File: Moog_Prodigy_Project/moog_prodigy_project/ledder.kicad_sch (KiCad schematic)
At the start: 44 parts, among them J6 NJ2FD-V, Q10 CA3046, Q11 BC327, Q8 BC556, Q9 CA3046, U1 LT1469, U15 LT1469, U16 LT1228, U17 NE5532

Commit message: Dodao u napomenu za linearne i logaritamske potenciometre, NE555 i sa 4007 semom spojena u jedno, dodati kvalitetni kondenzatori, ostao simbol za 4007 da izenim kao sto je jocke
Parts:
- added C77, C78: 100n, Capacitor_THT:CP_Radial_D5.0mm_P2.50mm, symbol Device:C
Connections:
- net +12V: now also C77.2, C78.2
- net GND: now also C77.1, C78.1
- net SIGNAL_OUT: no longer names the net of J6.S, RV16.2
- new net: Q8. (E), Q9., R97.2
- new net: CP1., Q9., R98.1
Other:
- note added: "IC1_1"
- note added: "IC1_2"
- note added: "IC1_3"
- note added: "IC1_4"
- note added: "IC1_5"
- note added: "IC2_1"
- note added: "IC2_2"
- note added: "IC2_3"
- note added: "IC2_4"
- note added: "IC2_5"
- note added: "NAPOMENA Kondenzatori: C71,C72,C73,C74,C75,C76,C77,C78 su vrednosti 100n i oni su kvalitetniji Ponteciometri: Linearni:RV12,RV15 Logaritamski: RV14,RV16"
- note added: "VOLUME MASTER"
- note removed: "NAPOMENA Kondenzatori: C71,C72,C73,C74,C75,C76 su vrednosti 100n i oni su kvalitetniji"
- title: (none) -> Dupli 3046 
- moved on the sheet: J6

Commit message: MOOG prodigy final 03.07.2026
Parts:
- R104, R105: value 6K81 -> 6K81 1%
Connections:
- new net: Q8. (E), Q9., R97.2
- new net: CP1., Q9., R98.1
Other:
- note added: "IC1"
- note added: "IC2"
- note added: "NAPOMENA 1 Kondenzatori: C71,C72,C73,C74,C75,C76,C77,C78 su vrednosti 100n i oni su kvalitetniji Ponteciometri: Linearni:RV12,RV15 Logaritamski: RV14,RV16"
- note added: "NAPOMENA 2 Otpornici cija je vrednost: 63K4, 18K2, 4K75, 6K81, 51M, 2.4M su otpornici iz E96 serije (1%) Ostali orpotnici su iz serije E24 (5%)"
- note removed: "NAPOMENA Kondenzatori: C71,C72,C73,C74,C75,C76,C77,C78 su vrednosti 100n i oni su kvalitetniji Ponteciometri: Linearni:RV12,RV15 Logaritamski: RV14,RV16"
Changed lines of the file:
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@@
 		(comment 4 "Miodrag Babić E1 87/2023")
 	)
+	(text "NAPOMENA 2\nOtpornici cija je vrednost:\n63K4, 18K2, 4K75, 6K81, 51M, 2.4M\nsu otpornici iz E96 serije (1%)\nOstali orpotnici su iz serije E24 (5%)"
+		(exclude_from_sim no)
+		(at 215.9 153.416 0)
+		(effects
+			(font
+				(size 1.27 1.27)
+				(thickness 0.254)
+				(bold yes)
+			)
+			(justify left)
+		)
+	)
 	(text "VCA\nBALANCE"
 		(exclude_from_sim no)
@@
 		)
 	)
-	(text "NAPOMENA\nKondenzatori:\nC71,C72,C73,C74,C75,C76,C77,C78\nsu vrednosti 100n i oni su kvalitetniji\n\nPonteciometri:\nLinearni:RV12,RV15\nLogaritamski: RV14,RV16"
+	(text "NAPOMENA 1\nKondenzatori:\nC71,C72,C73,C74,C75,C76,C77,C78\nsu vrednosti 100n i oni su kvalitetniji\n\nPonteciometri:\nLinearni:RV12,RV15\nLogaritamski: RV14,RV16"
 		(exclude_from_sim no)
-		(at 236.474 154.178 0)
+		(at 176.784 156.21 0)
 		(effects
 			(font
@@
 		)
 	)
+	(text "IC1"
+		(exclude_from_sim no)
+		(at 41.402 68.072 0)
+		(effects
+			(font
+				(size 1.27 1.27)
+			)
+		)
+	)
 	(text "IC2_2"
 		(exclude_from_sim no)
@@
 		)
 	)
+	(text "IC2"
+		(exclude_from_sim no)
+		(at 167.386 65.024 0)
+		(effects
+			(font
+				(size 1.27 1.27)
+			)
+		)
+	)
 	(text "EMPHASIS"
 		(exclude_from_sim no)
@@
 		)
 		(property "Value" "CA3046"
-			(at 50.038 76.962 90)
+			(at 41.91 70.358 90)
 			(effects
 				(font
@@
 		(dnp no)
 		(property "Reference" "R104"
-			(at 136.144 111.252 0)
+			(at 135.382 112.268 0)
 			(effects
 				(font
@@
 			)
 		)
-		(property "Value" "6K81"
-			(at 136.144 113.792 0)
+		(property "Value" "6K81 1%"
+			(at 131.826 114.554 0)
 			(effects
 				(font
@@
 			)
 		)
-		(property "Value" "6K81"
-			(at 151.384 120.142 90)
+		(property "Value" "6K81 1%"
+			(at 149.606 120.142 90)
 			(effects
 				(font

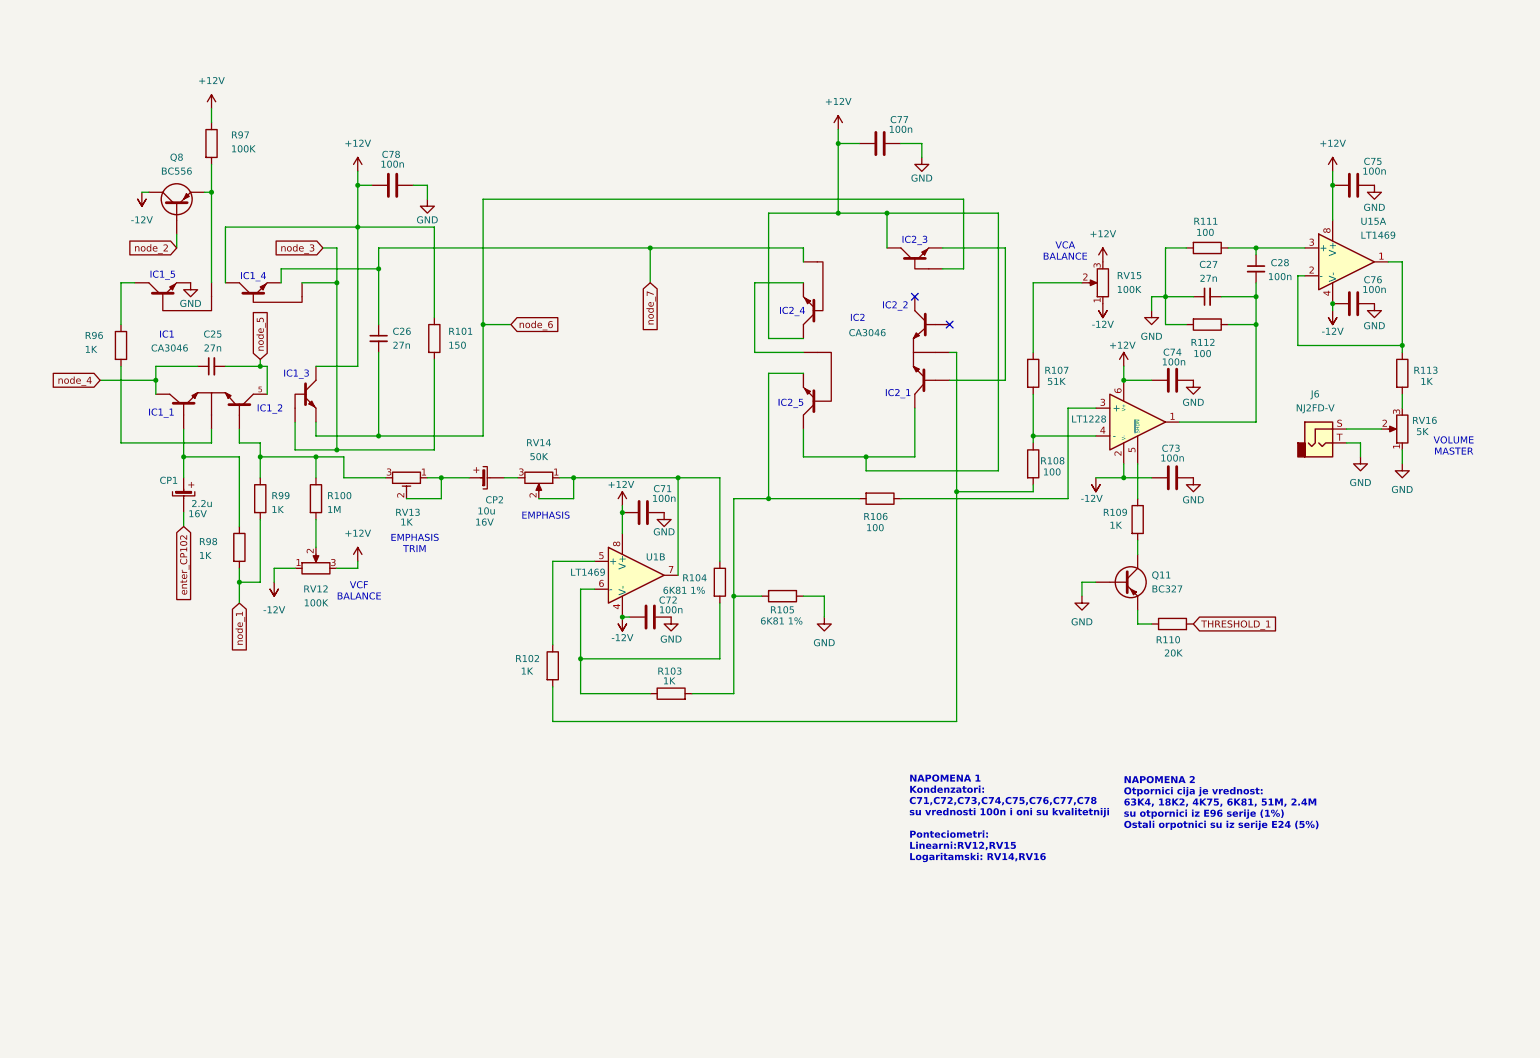
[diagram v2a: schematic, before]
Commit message: Moog prodigy fix 3
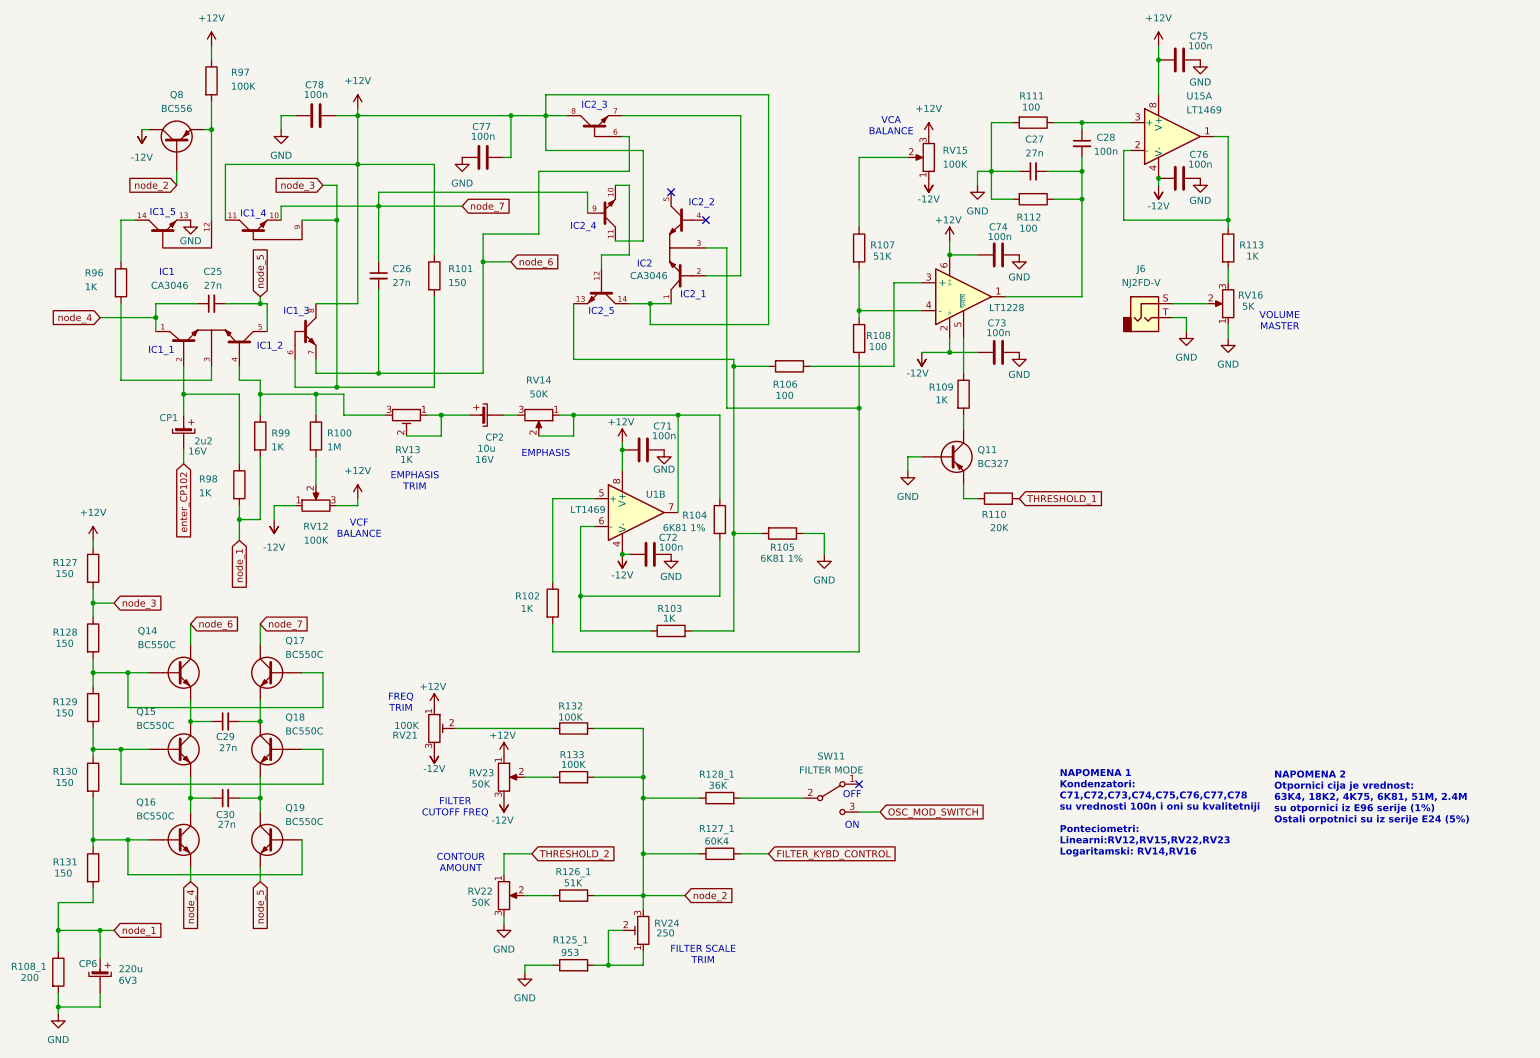
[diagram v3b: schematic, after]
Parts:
- added C29, C30: 27n, Capacitor_THT:C_Disc_D3.8mm_W2.6mm_P2.50mm, symbol Device:C_Small
- added CP6: 220u, Capacitor_THT:CP_Radial_D5.0mm_P2.50mm, symbol elektrolitski:elektrolit
- added Q14, Q15, Q16, Q17, Q18, Q19: BC550C, Package_TO_SOT_THT:TO-92_Inline, symbol Transistor_BJT:BC550
- added R108_1: 200, Resistor_THT:R_Axial_DIN0207_L6.3mm_D2.5mm_P7.62mm_Horizontal, symbol Device:R
- added R125_1: 953, Resistor_THT:R_Axial_DIN0207_L6.3mm_D2.5mm_P7.62mm_Horizontal, symbol Device:R
- added R126_1: 51K, Resistor_THT:R_Axial_DIN0207_L6.3mm_D2.5mm_P7.62mm_Horizontal, symbol Device:R
- added R127, R128, R129, R130, R131: 150, Resistor_THT:R_Axial_DIN0207_L6.3mm_D2.5mm_P7.62mm_Horizontal, symbol Device:R
- added R127_1: 60K4, Resistor_THT:R_Axial_DIN0207_L6.3mm_D2.5mm_P7.62mm_Horizontal, symbol Device:R
- added R128_1: 36K, Resistor_THT:R_Axial_DIN0207_L6.3mm_D2.5mm_P7.62mm_Horizontal, symbol Device:R
- added R132, R133: 100K, Resistor_THT:R_Axial_DIN0207_L6.3mm_D2.5mm_P7.62mm_Horizontal, symbol Device:R
- added RV21: 100K, Potentiometer_THT:Potentiometer_ACP_CA9-V10_Vertical, symbol Device:R_Potentiometer_Trim
- added RV22, RV23: 50K, Potentiometer_THT:Potentiometer_ACP_CA9-V10_Vertical, symbol Device:R_Potentiometer
- added RV24: 250, Potentiometer_THT:Potentiometer_Bourns_3339P_Vertical_HandSoldering, symbol Device:R_Potentiometer_Trim
- added SW11: FILTER MODE, ATE1D-2M3-10-Z_1x2:SW_ATE1D-2M3-10-Z, symbol Switch:SW_SPDT
- CP1: value 2.2u -> 2u2
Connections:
- net +12V: now also C77.1, C78.1, Q10.1, Q10.11, Q10.14, Q10.8, Q9.11, Q9.8, R127.1, RV21.1, RV23.1; no longer C77.2, C78.2, Q10., Q9.
- net -12V: now also RV21.3, RV23.3
- net GND: now also C77.2, C78.2, Q9.13, CP6., R108_1.2, R125_1.1, RV22.3; no longer C77.1, C78.1, Q9.
- net node_1: now also CP6., R108_1.1, R131.2
- net node_2: now also R126_1.2, R127_1.1, R128_1.1, R132.2, R133.2, RV24.3
- net node_3: now also Q9.6, Q9.9, R127.2, R128.1; no longer Q9.
- net node_4: now also Q9.1, Q16. (E); no longer Q9.
- net node_5: now also Q19. (E)
- net node_6: now also Q10.6, Q9.7, Q14. (E); no longer Q10., Q9.
- net node_7: now also Q10.9, Q9.10, Q17. (E); no longer Q10., Q9.
- net at R102.2, R108.2: now also Q10.3; no longer Q10.
- net at R100.1, R99.1, RV13.3: now also Q9.4; no longer Q9.
- net at R96.1: now also Q9.14; no longer Q9.
- net at R96.2: now also Q9.3; no longer Q9.
- net at R103.2, R105.2, R106.2: now also Q10.13; no longer Q10.
- new net: R133.1, RV23.2
- new net: C29.2, Q17. (E), Q18. (E)
- new net: Q14. (E), Q17. (E), R128.2, R129.1
- new net: R128_1.2, SW11.2 (B)
- new net: C29.1, Q14. (E), Q15. (E)
- new net: Q8. (E), Q9.12, R97.2
- new net: Q15. (E), Q18. (E), R129.2, R130.1
- new net: R126_1.1, RV22.2
- new net: C30.1, Q15. (E), Q16. (E)
- new net: CP1., Q9.2, R98.1
- new net: Q10.10, Q10.12
- new net: Q10.2, Q10.7
- new net: Q16. (E), Q19. (E), R130.2, R131.1
- new net: R132.1, RV21.2
- new net: C30.2, Q18. (E), Q19. (E)
- new net: R125_1.2, RV24.1, RV24.2
- new net FILTER_KYBD_CONTROL: R127_1.2
- new net OSC_MOD_SWITCH: SW11.3 (C)
- new net THRESHOLD_2: RV22.1
- no-connect marks 2 -> 3
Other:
- note added: "CONTOUR AMOUNT"
- note added: "FILTER CUTOFF FREQ"
- note added: "FILTER SCALE TRIM"
- note added: "FREQ TRIM"
- note added: "NAPOMENA 1 Kondenzatori: C71,C72,C73,C74,C75,C76,C77,C78 su vrednosti 100n i oni su kvalitetniji Ponteciometri: Linearni:RV12,RV15,RV22,RV23 Logaritamski: RV14,RV16"
- note added: "OFF"
- note added: "ON"
- note removed: "NAPOMENA 1 Kondenzatori: C71,C72,C73,C74,C75,C76,C77,C78 su vrednosti 100n i oni su kvalitetniji Ponteciometri: Linearni:RV12,RV15 Logaritamski: RV14,RV16"
- moved on the sheet: C25, C26, C27, C28, C71, C72, C73, C74, C75, C76, C78, CP1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
